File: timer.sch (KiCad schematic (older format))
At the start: 8 parts, among them IC56 8253, IC69 74LS74, IC84 74LS00, Q1 2N3904

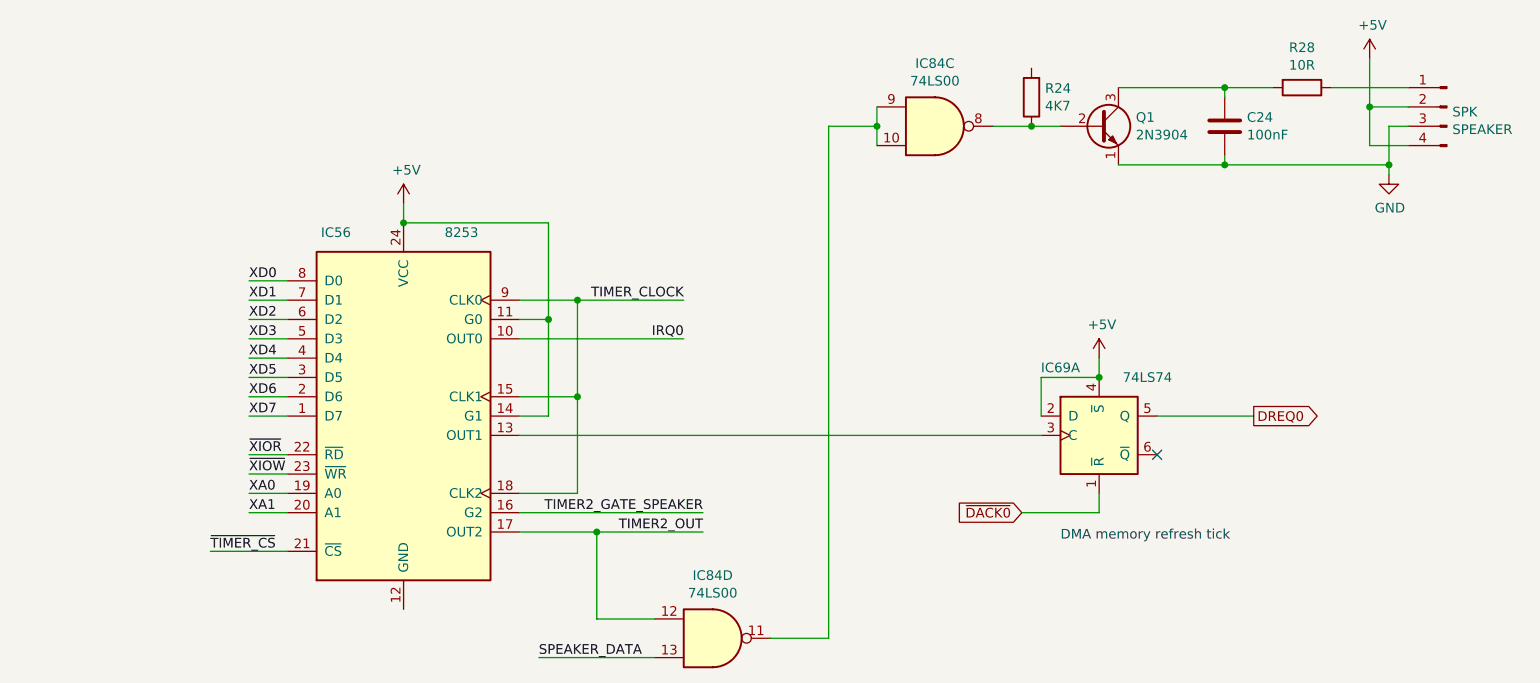
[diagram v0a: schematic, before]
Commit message: Tidy up and map all signals
This fixes up the schematic to:
 - Look presentable
 - Fix all labels connecting sheets
 - Tidy up all loose ends by either inspecting the PCB under
    magnification, measuring with an oscillosope or buzzing
    out with a meter
 - Pass ERC (with 1 exception due to incorrect circuitry around
    pin 33 on the FPU (~RQ~/~GT1~)
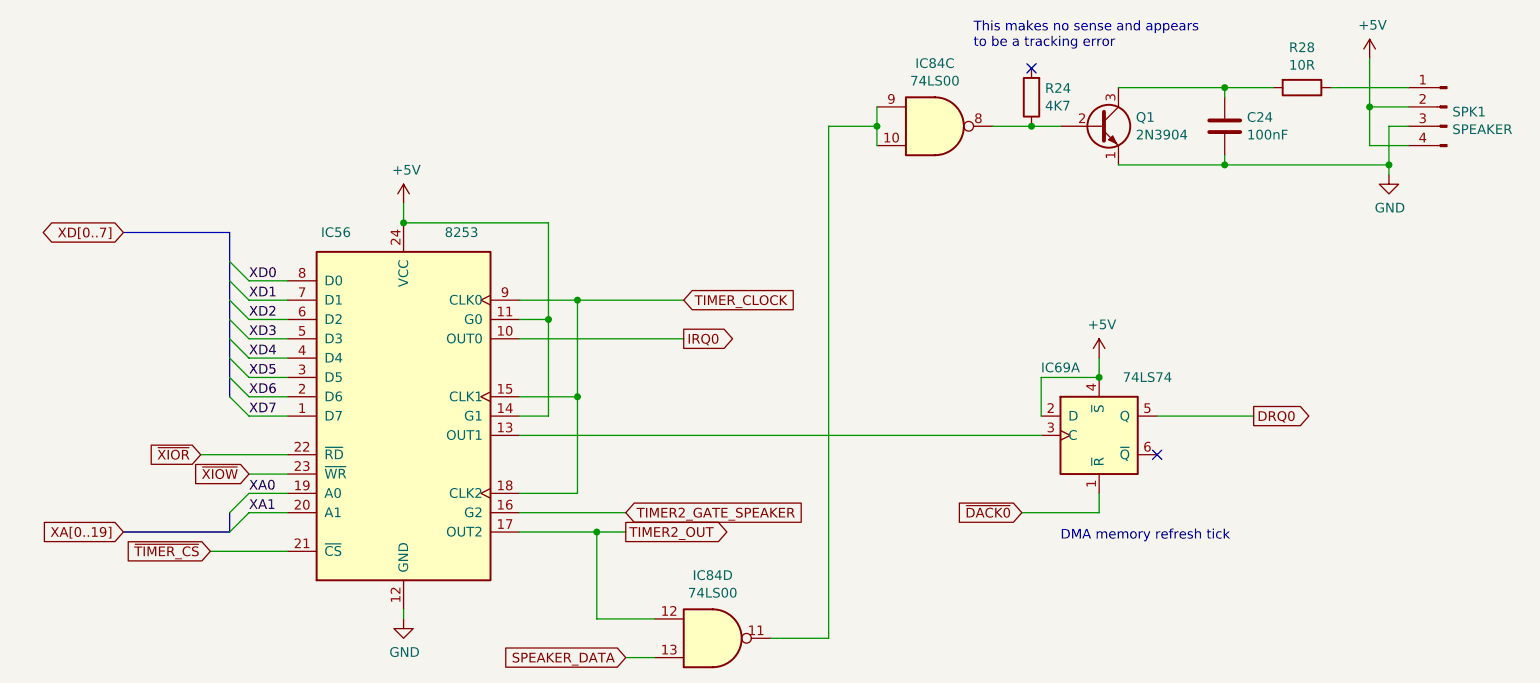
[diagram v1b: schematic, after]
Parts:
- renumbered SPK to SPK1
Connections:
- net GND: now also IC56.12 (GND)
- net DREQ0 renamed DRQ0
- no-connect marks 1 -> 2
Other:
- note added: "This makes no sense and appears \nto be a tracking error"
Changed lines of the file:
@@
 $Descr A4 11693 8268
 encoding utf-8
-Sheet 13 13
-Title ""
+Sheet 13 16
+Title "Wugo PCII System Board"
 Date ""
 Rev ""
@@
 $EndComp
 $Comp
-L Connector:Conn_01x04_Male SPK
+L Connector:Conn_01x04_Male SPK1
 U 1 1 5F2EBFC8
 P 8200 2100
-F 0 "SPK" H 8172 2074 50  0000 R CNN
+F 0 "SPK1" H 8172 2074 50  0000 R CNN
 F 1 "SPEAKER" H 8172 1983 50  0000 R CNN
 F 2 "" H 8200 2100 50  0001 C CNN
@@
 $EndComp
 $Comp
-L power:+5V #PWR?
+L power:+5V #PWR086
 U 1 1 5F2ECC14
 P 7800 1850
-F 0 "#PWR?" H 7800 1700 50  0001 C CNN
+F 0 "#PWR086" H 7800 1700 50  0001 C CNN
 F 1 "+5V" H 7815 2023 50  0000 C CNN
 F 2 "" H 7800 1850 50  0001 C CNN
@@
 	7800 2100 7800 1850
 $Comp
-L power:GND #PWR?
+L power:GND #PWR087
 U 1 1 5F2ED3A7
 P 7900 2450
-F 0 "#PWR?" H 7900 2200 50  0001 C CNN
+F 0 "#PWR087" H 7900 2200 50  0001 C CNN
 F 1 "GND" H 7905 2277 50  0000 C CNN
 F 2 "" H 7900 2450 50  0001 C CNN
@@
 	5850 2200 6050 2200
 Connection ~ 6050 2200
-Text Label 2000 3900 0    50   ~ 0
-~XIOR~
-Text Label 2000 4000 0    50   ~ 0
-~XIOW~
 Text Label 2000 3000 0    50   ~ 0
 XD0
@@
 	2000 3700 2200 3700
 Wire Wire Line
-	2000 3900 2200 3900
+	1750 3900 2200 3900
 Wire Wire Line
 	2000 4000 2200 4000
@@
 Text Label 2000 4200 0    50   ~ 0
 XA1
-Text Label 1800 4400 0    50   ~ 0
-~TIMER_CS~
-Wire Wire Line
-	1800 4400 2200 4400
 Wire Wire Line
 	4250 3300 3400 3300
-Text Label 4250 3300 2    50   ~ 0
-IRQ0
 Wire Wire Line
 	3400 3700 3550 3700
@@
 	3700 4100 3400 4100
 Connection ~ 3700 3600
-Text Label 4250 3100 2    50   ~ 0
-TIMER_CLOCK
 Text GLabel 7200 3700 2    50   Output ~ 0
-DREQ0
+DRQ0
 Text Notes 6200 4350 0    50   ~ 0
 DMA memory refresh tick
@@
 $EndComp
 $Comp
-L power:+5V #PWR?
+L power:+5V #PWR085
 U 1 1 5F38DC92
 P 6400 3400
-F 0 "#PWR?" H 6400 3250 50  0001 C CNN
+F 0 "#PWR085" H 6400 3250 50  0001 C CNN
 F 1 "+5V" H 6415 3573 50  0000 C CNN
 F 2 "" H 6400 3400 50  0001 C CNN
@@
 Connection ~ 6400 3500
 $Comp
-L power:+5V #PWR?
+L power:+5V #PWR084
 U 1 1 5F3919C0
 P 2800 2600
-F 0 "#PWR?" H 2800 2450 50  0001 C CNN
+F 0 "#PWR084" H 2800 2450 50  0001 C CNN
 F 1 "+5V" H 2815 2773 50  0000 C CNN
 F 2 "" H 2800 2600 50  0001 C CNN
@@
 	2800 2600 2800 2700
 Connection ~ 2800 2700
-Text Label 4350 4200 2    50   ~ 0
-TIMER2_GATE_SPEAKER
-Wire Wire Line
-	3400 4200 4350 4200
+Wire Wire Line
+	3400 4200 3950 4200
 $Comp
 L 74xx:74LS00 IC84
@@
 Wire Wire Line
 	5000 2200 5000 4850
-Text Label 3500 4950 0    50   ~ 0
+Wire Wire Line
+	3950 4950 4100 4950
+Wire Wire Line
+	3800 4300 3950 4300
+Connection ~ 3800 4300
+Text GLabel 1800 4400 0    50   Input ~ 0
+~TIMER_CS~
+Text GLabel 1750 3900 0    50   Input ~ 0
+~XIOR~
+Text GLabel 2000 4000 0    50   Input ~ 0
+~XIOW~
+Entry Wire Line
+	1900 4300 2000 4200
+Entry Wire Line
+	1900 4200 2000 4100
+Wire Wire Line
+	1800 4400 2200 4400
+Wire Bus Line
+	1900 4200 1900 4300
+Wire Bus Line
+	1900 4300 1350 4300
+Text GLabel 1350 4300 0    50   Input ~ 0
+XA[0..19]
+Entry Wire Line
+	1900 2900 2000 3000
+Entry Wire Line
+	1900 3000 2000 3100
+Entry Wire Line
+	1900 3100 2000 3200
+Entry Wire Line
+	1900 3200 2000 3300
+Entry Wire Line
+	1900 3300 2000 3400
+Entry Wire Line
+	1900 3400 2000 3500
+Entry Wire Line
+	1900 3500 2000 3600
+Entry Wire Line
+	1900 3600 2000 3700
+Wire Bus Line
+	1900 2750 1350 2750
+Text GLabel 1350 2750 0    50   3State ~ 0
+XD[0..7]
+$Comp
+L power:GND #PWR0137
+U 1 1 61391A6C
+P 2800 4750
+F 0 "#PWR0137" H 2800 4500 50  0001 C CNN
+F 1 "GND" H 2805 4577 50  0000 C CNN
+F 2 "" H 2800 4750 50  0001 C CNN
+F 3 "" H 2800 4750 50  0001 C CNN
+	1    2800 4750
+	1    0    0    -1
+$EndComp
+Wire Wire Line
+	2800 4700 2800 4750
+NoConn ~ 6050 1900
+Text Notes 5750 1800 0    50   ~ 0
+This makes no sense and appears \nto be a tracking error
+Text GLabel 4250 3100 2    50   Input ~ 0
+TIMER_CLOCK
+Text GLabel 4250 3300 2    50   Output ~ 0
+IRQ0
+Text GLabel 3950 4200 2    50   Input ~ 0
+TIMER2_GATE_SPEAKER
+Text GLabel 3950 4300 2    50   Output ~ 0
+TIMER2_OUT
+Text GLabel 3950 4950 0    50   Input ~ 0
 SPEAKER_DATA
-Wire Wire Line
-	3500 4950 4100 4950
-Text Label 4350 4300 2    50   ~ 0
-TIMER2_OUT
-Wire Wire Line
-	3800 4300 4350 4300
-Connection ~ 3800 4300
+Wire Bus Line
+	1900 2750 1900 3600
 $EndSCHEMATC
